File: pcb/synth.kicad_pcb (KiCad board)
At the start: 2 copper layers, 97.4 x 69.1 mm, 68 parts, among them J1 Conn_01x06, J2 Barrel_Jack_Switch, SW1 SW_Push, SW10 SW_Push, SW11 SW_Push, SW12 SW_Push, SW13 SW_Push, SW14 SW_Push, SW15 SW_Push, SW16 SW_Push, SW17 SW_Push, SW18 SW_Push, SW19 SW_Push, SW2 SW_Push, SW20 SW_Push, SW21 SW_Push, SW22 SW_Push, SW23 SW_Push, SW24 SW_Push, SW25 SW_Push, SW26 SW_Push, SW27 SW_Push, SW28 SW_Push, SW29 SW_Push, SW3 SW_Push, SW30 SW_Push, SW4 SW_Push, SW5 SW_Push, SW6 SW_Push, SW7 SW_Push, SW8 SW_Push, SW9 SW_Push, U1 LD1117S33TR_SOT223, U2 STM32F407VGTx, Y1 Crystal_8

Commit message: A bunch of routing and footprint changes.
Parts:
- C1, C10, C11, C12, C13, C14, C15, C16, C18, C19, C2, C3, C4, C5, C6, C7, C8: footprint Capacitor_THT:CP_Axial_L11.0mm_D8.0mm_P15.00mm_Horizontal -> Capacitor_THT:C_Disc_D3.0mm_W2.0mm_P2.50mm
- R2, R3: footprint Resistor_THT:R_Axial_DIN0207_L6.3mm_D2.5mm_P2.54mm_Vertical -> Resistor_THT:R_Axial_DIN0204_L3.6mm_D1.6mm_P5.08mm_Horizontal
- RV1, RV2, RV3, RV4, RV5, RV6, RV7, RV8: footprint Potentiometer_THT:Potentiometer_Bourns_3005_Horizontal -> Potentiometer_THT:Potentiometer_Bourns_PTV09A-1_Single_Vertical
- Y1: footprint Crystal:Crystal_AT310_D3.0mm_L10.0mm_Horizontal -> Synth_Footprints:ATS08A
- moved J1 176.0 mm to (91.9, 83.6)
- moved RV6 160.3 mm to (71.4, 118.1), turned to 90 degrees
- moved C19 146.1 mm to (139.7, 93.1), turned to 90 degrees
- moved C15 138.3 mm to (197.1, 99.6)
- moved C14 135.4 mm to (196.4, 107.4)
- moved RV8 135.2 mm to (72.1, 101.6), turned to 90 degrees
- moved C16 130.8 mm to (129.5, 97.7), turned to 180 degrees
- moved C18 130.2 mm to (143.0, 93.1), turned to 90 degrees
- moved R3 125.6 mm to (158.0, 110.5)
- moved C5 113.4 mm to (137.1, 93.1), turned to 90 degrees
- moved RV1 103.1 mm to (104.1, 85.6), turned to 90 degrees
- moved C3 96.6 mm to (149.1, 93.0), turned to 90 degrees
- moved C2 93.8 mm to (130.3, 114.8), turned to 180 degrees
- moved RV2 87.2 mm to (119.4, 85.6), turned to 90 degrees
- moved RV4 80.7 mm to (146.3, 85.6), turned to 90 degrees
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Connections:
- SW1 pad 2: C1 -> /C1
- SW10 pad 2: A1 -> /A1
- SW11 pad 2: A#1 -> /A#1
- SW12 pad 2: B1 -> /B1
- SW13 pad 2: C2 -> /C2
- SW14 pad 2: C#2 -> /C#2
- SW15 pad 2: D2 -> /D2
- SW16 pad 2: D#2 -> /D#2
- SW17 pad 2: E2 -> /E2
- SW18 pad 2: F2 -> /F2
- SW19 pad 2: F#2 -> /F#2
- SW2 pad 2: C#1 -> /C#1
- SW20 pad 2: G2 -> /G2
- SW21 pad 2: G#2 -> /G#2
- SW22 pad 2: A2 -> /A2
- SW23 pad 2: A#2 -> /A#2
- SW24 pad 2: B2 -> /B2
- SW3 pad 2: D1 -> /D1
- SW4 pad 2: D#1 -> /D#1
- SW5 pad 2: E1 -> /E1
- SW6 pad 2: F1 -> /F1
- SW7 pad 2: F#1 -> /F#1
- SW8 pad 2: G1 -> /G1
- SW9 pad 2: G#1 -> /G#1
- U2 pad 1: D1 -> Net-(U2-Pad1)
- U2 pad 2: D#1 -> Net-(U2-Pad2)
- U2 pad 3: E1 -> Net-(U2-Pad3)
- U2 pad 38: G1 -> Net-(U2-Pad38)
- U2 pad 39: G#1 -> Net-(U2-Pad39)
- U2 pad 4: F1 -> Net-(U2-Pad4)
- U2 pad 40: A1 -> Net-(U2-Pad40)
- U2 pad 41: A#1 -> Net-(U2-Pad41)
- U2 pad 42: B1 -> Net-(U2-Pad42)
- U2 pad 43: C2 -> Net-(U2-Pad43)
- U2 pad 44: C#2 -> Net-(U2-Pad44)
- U2 pad 45: D2 -> /C1
- U2 pad 46: D#2 -> /C#1
- U2 pad 47: Net-(U2-Pad47) -> /D1
- U2 pad 48: Net-(U2-Pad48) -> /D#1
- U2 pad 5: F#1 -> Net-(U2-Pad5)
- U2 pad 51: Net-(U2-Pad51) -> /E1
- U2 pad 52: Net-(U2-Pad52) -> /F1
- U2 pad 53: Net-(U2-Pad53) -> /F#1
- U2 pad 54: Net-(U2-Pad54) -> /G1
- U2 pad 55: /VOLUME -> /G#1
- U2 pad 56: /ATTACK -> /A1
- U2 pad 57: /DECAY -> /A#1
- U2 pad 58: /SUSTAIN -> /B1
- U2 pad 59: /RELEASE -> /C2
- U2 pad 60: /GLIDE_SPEED -> /C#2
- U2 pad 61: /MIXER_AMT -> /D2
- U2 pad 62: /WAVE_SHAPE -> /D#2
- U2 pad 63: Net-(U2-Pad63) -> /E2
- U2 pad 65: Net-(U2-Pad65) -> /F2
- U2 pad 66: Net-(U2-Pad66) -> /F#2
- U2 pad 67: Net-(U2-Pad67) -> /G2
- U2 pad 68: Net-(U2-Pad68) -> /G#2
- U2 pad 69: Net-(U2-Pad69) -> /A2
- U2 pad 70: Net-(U2-Pad70) -> /A#2
- U2 pad 71: Net-(U2-Pad71) -> /B2
- U2 pad 81: E2 -> Net-(U2-Pad81)
- U2 pad 82: F2 -> Net-(U2-Pad82)
- U2 pad 83: F#2 -> Net-(U2-Pad83)
- U2 pad 84: G2 -> Net-(U2-Pad84)
- U2 pad 85: G#2 -> Net-(U2-Pad85)
- U2 pad 86: A2 -> Net-(U2-Pad86)
- U2 pad 87: A#2 -> Net-(U2-Pad87)
- U2 pad 88: B2 -> Net-(U2-Pad88)
- U2 pad 97: C1 -> Net-(U2-Pad97)
- U2 pad 98: C#1 -> Net-(U2-Pad98)
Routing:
- net +3V3: track 137.2 -> 301.7 mm
- net /C1: track 0.00 -> 50.1 mm
- net /B2: track 0.00 -> 46.8 mm
- net /D1: track 0.00 -> 46.7 mm
- net /A2: track 0.00 -> 42.4 mm
- net /C#1: track 0.00 -> 38.8 mm
- net /G2: track 0.00 -> 37.9 mm
- net /A#2: track 0.00 -> 35.8 mm
- net /D#1: track 0.00 -> 35.1 mm
- net /E1: track 0.00 -> 34.5 mm
- net /F1: track 0.00 -> 32.4 mm
- net /F2: track 0.00 -> 32.3 mm
- net /G#2: track 0.00 -> 31.3 mm
- net /E2: track 0.00 -> 30.3 mm
- net /G1: track 0.00 -> 29.9 mm
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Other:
- net class Power: trace_width 0.5 -> 0.25

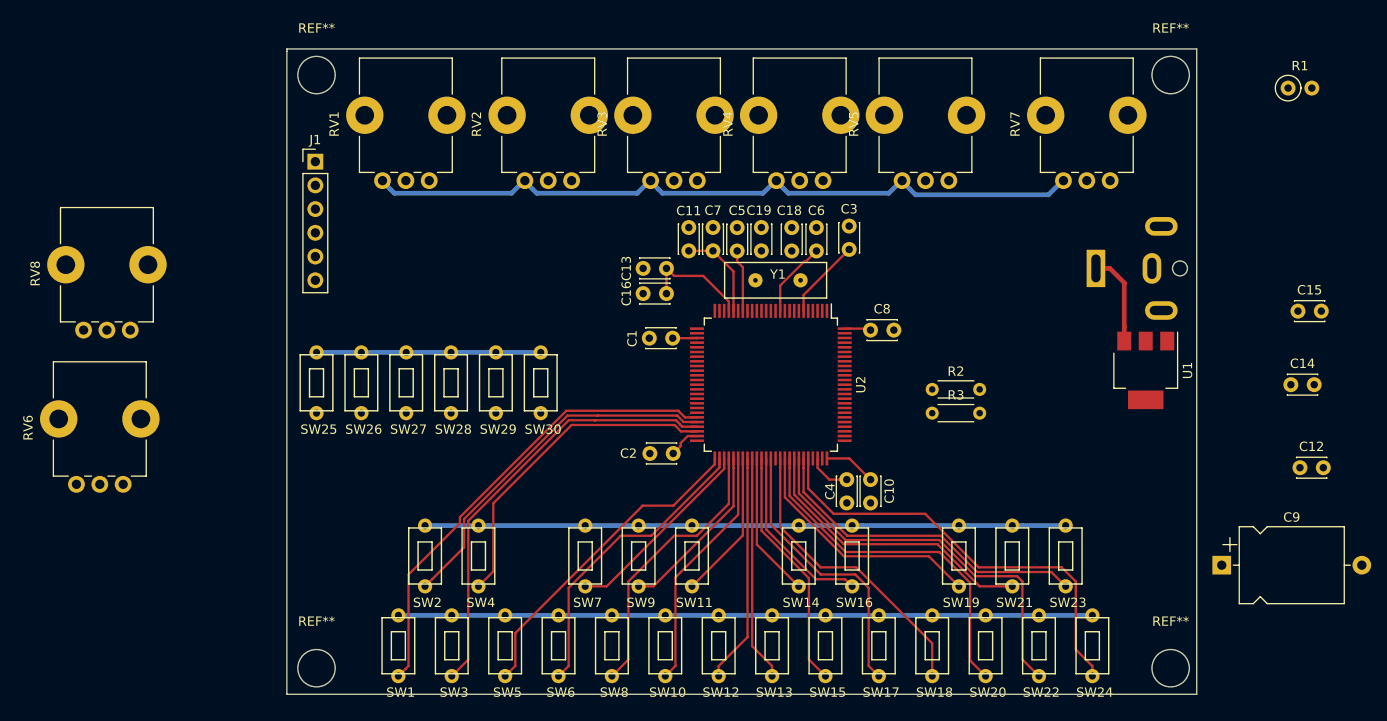
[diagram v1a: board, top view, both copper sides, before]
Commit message: A ton of changes.
- Redid the routing for the keyboard.
- Added LEDs for Arp style and scale with accompanying driver.
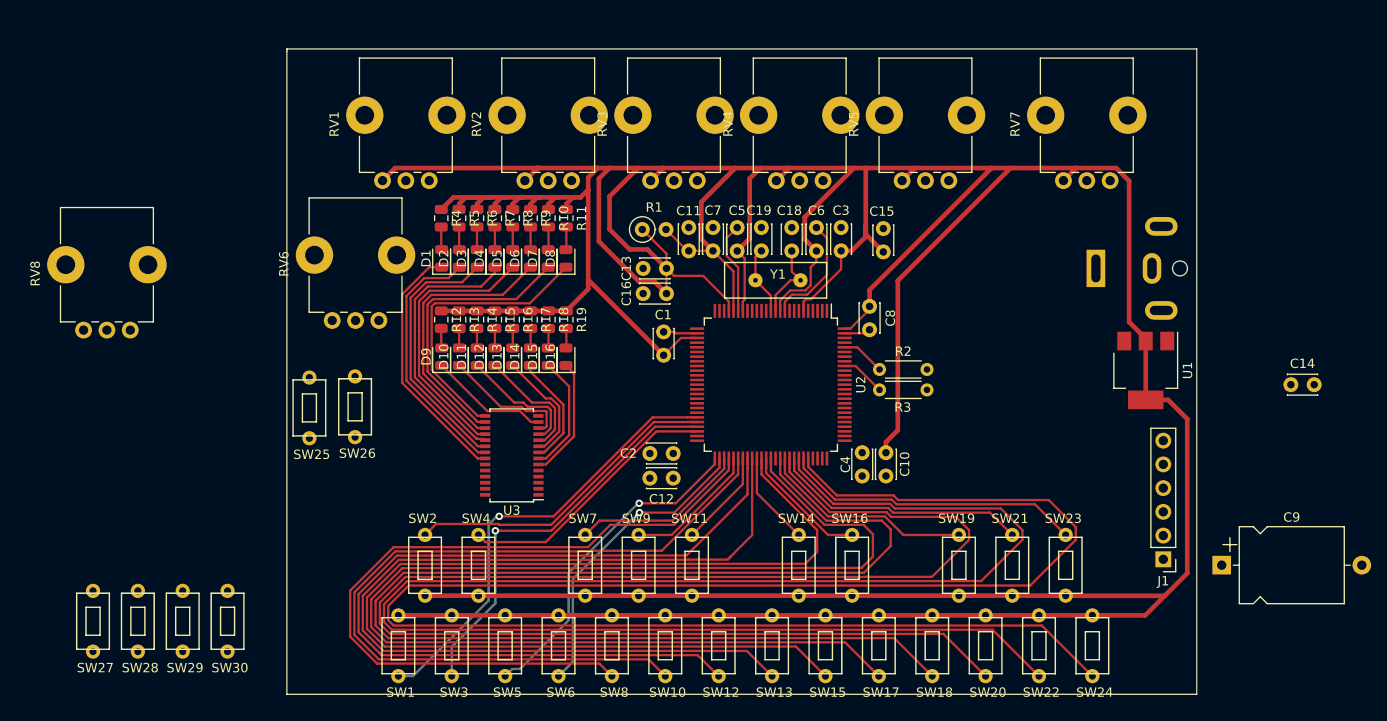
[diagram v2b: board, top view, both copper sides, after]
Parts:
- removed REF** (x4): MountingHole_4mm, MountingHole:MountingHole_4mm
- added D1: LED_Small, LED_SMD:LED_0805_2012Metric, F.Cu at (105.5, 93.9)
- added D10: LED_Small, LED_SMD:LED_0805_2012Metric, F.Cu at (107.4, 104.5)
- added D11: LED_Small, LED_SMD:LED_0805_2012Metric, F.Cu at (109.3, 104.5)
- added D12: LED_Small, LED_SMD:LED_0805_2012Metric, F.Cu at (111.2, 104.5)
- added D13: LED_Small, LED_SMD:LED_0805_2012Metric, F.Cu at (113.1, 104.5)
- added D14: LED_Small, LED_SMD:LED_0805_2012Metric, F.Cu at (115.0, 104.5)
- added D15: LED_Small, LED_SMD:LED_0805_2012Metric, F.Cu at (116.9, 104.5)
- added D16: LED_Small, LED_SMD:LED_0805_2012Metric, F.Cu at (118.8, 104.5)
- added D2: LED_Small, LED_SMD:LED_0805_2012Metric, F.Cu at (107.4, 93.9)
- added D3: LED_Small, LED_SMD:LED_0805_2012Metric, F.Cu at (109.3, 93.9)
- added D4: LED_Small, LED_SMD:LED_0805_2012Metric, F.Cu at (111.2, 93.9)
- added D5: LED_Small, LED_SMD:LED_0805_2012Metric, F.Cu at (113.1, 93.9)
- added D6: LED_Small, LED_SMD:LED_0805_2012Metric, F.Cu at (115.0, 93.9)
- added D7: LED_Small, LED_SMD:LED_0805_2012Metric, F.Cu at (116.9, 93.9)
- added D8: LED_Small, LED_SMD:LED_0805_2012Metric, F.Cu at (118.8, 93.9)
- added D9: LED_Small, LED_SMD:LED_0805_2012Metric, F.Cu at (105.5, 104.5)
- added R10: 220, Resistor_SMD:R_0805_2012Metric, F.Cu at (116.9, 89.6)
- added R11: 220, Resistor_SMD:R_0805_2012Metric, F.Cu at (118.8, 89.6)
- added R12: 220, Resistor_SMD:R_0805_2012Metric, F.Cu at (105.4, 100.5)
- added R13: 220, Resistor_SMD:R_0805_2012Metric, F.Cu at (107.3, 100.5)
- added R14: 220, Resistor_SMD:R_0805_2012Metric, F.Cu at (109.3, 100.5)
- added R15: 220, Resistor_SMD:R_0805_2012Metric, F.Cu at (111.2, 100.5)
- added R16: 220, Resistor_SMD:R_0805_2012Metric, F.Cu at (113.1, 100.5)
- added R17: 220, Resistor_SMD:R_0805_2012Metric, F.Cu at (115.0, 100.5)
- added R18: 220, Resistor_SMD:R_0805_2012Metric, F.Cu at (116.9, 100.5)
- added R19: 220, Resistor_SMD:R_0805_2012Metric, F.Cu at (118.8, 100.5)
- added R4: 220, Resistor_SMD:R_0805_2012Metric, F.Cu at (105.4, 89.6)
- added R5: 220, Resistor_SMD:R_0805_2012Metric, F.Cu at (107.3, 89.6)
- added R6: 220, Resistor_SMD:R_0805_2012Metric, F.Cu at (109.3, 89.6)
- added R7: 220, Resistor_SMD:R_0805_2012Metric, F.Cu at (111.2, 89.6)
- added R8: 220, Resistor_SMD:R_0805_2012Metric, F.Cu at (113.1, 89.6)
- added R9: 220, Resistor_SMD:R_0805_2012Metric, F.Cu at (115.0, 89.6)
- added U3: PCA9685PW, Package_SO:TSSOP-28_4.4x9.7mm_P0.65mm, F.Cu at (113.0, 115.0)
- moved J1 100.3 mm to (182.7, 126.1), turned to 180 degrees
- moved R1 70.8 mm to (126.9, 90.8)
- moved C12 67.1 mm to (130.3, 117.4), turned to 180 degrees
- moved C15 44.8 mm to (152.8, 93.2), turned to 90 degrees
- moved SW29 42.1 mm to (77.7, 133.3)
- moved SW30 42.1 mm to (82.5, 133.3)
- moved SW27 42.1 mm to (68.1, 133.3)
- moved SW28 42.1 mm to (72.9, 133.3)
- moved RV6 32.5 mm to (98.8, 100.6)
- moved R3 6.16 mm to (152.3, 108.0)
- moved R2 6.03 mm to (152.3, 105.8)
- moved C10 3.32 mm to (153.0, 114.7)
- moved C4 3.32 mm to (150.5, 114.7)
- moved SW25 2.80 mm to (91.3, 110.4)
- moved SW26 2.66 mm to (96.2, 110.3)
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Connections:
- net /BUTTON_1 renamed /GLIDE_SHAPE
- net /GLIDE_SPEED renamed /ARP_SPEED
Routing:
- net +3V3: track 301.7 -> 573.9 mm
- net /B2: track 46.8 -> 189.5 mm
- net /A2: track 42.4 -> 174.5 mm
- net /G2: track 37.9 -> 159.6 mm
- net /F2: track 32.3 -> 139.8 mm
- net /E2: track 30.3 -> 132.6 mm
- net /D2: track 26.1 -> 117.2 mm
- net /C2: track 24.2 -> 102.5 mm
- net /B1: track 24.6 -> 94.7 mm
- net /A1: track 26.5 -> 87.7 mm
- net /G1: track 29.9 -> 81.8 mm
- net /ARP_STYLE_LED_7: track 0.00 -> 30.7 mm
- net /ARP_STYLE_LED_6: track 0.00 -> 30.2 mm
- net /ARP_STYLE_LED_5: track 0.00 -> 29.7 mm
- net /ARP_STYLE_LED_4: track 0.00 -> 29.3 mm
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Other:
- net class Power: trace_width 0.25 -> 0.5

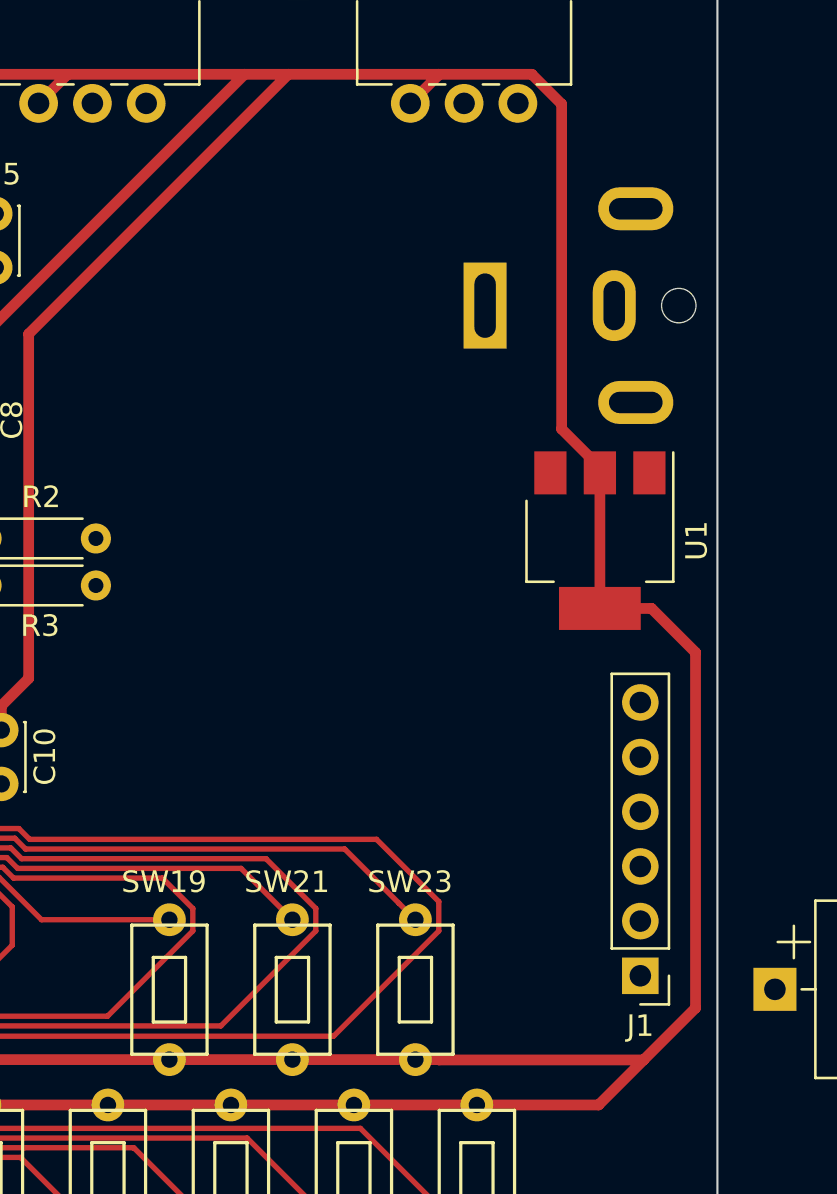
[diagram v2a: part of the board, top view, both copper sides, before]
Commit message: Add CS43L22 audio DAC.
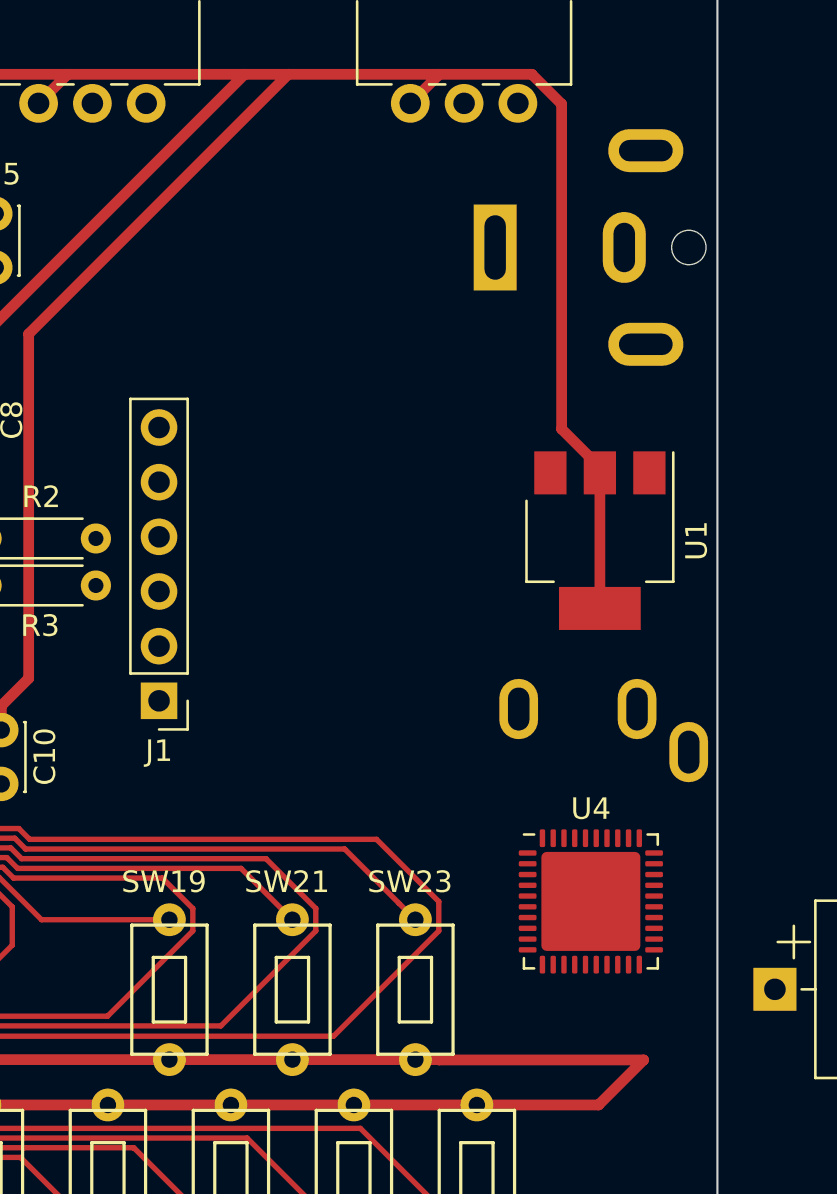
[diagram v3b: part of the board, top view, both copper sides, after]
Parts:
- added J3: AudioJack3, Connector_Audio:Jack_3.5mm_CUI_SJ1-3533NG_Horizontal, B.Cu at (185.0, 115.7)
- added U4: CS43L22, Package_DFN_QFN:QFN-40-1EP_6x6mm_P0.5mm_EP4.6x4.6mm, F.Cu at (180.4, 122.7)
- moved J1 25.8 mm to (160.4, 113.4)
- moved J2 2.74 mm to (176.0, 92.3)
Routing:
- net +3V3: track 573.9 -> 548.7 mm
